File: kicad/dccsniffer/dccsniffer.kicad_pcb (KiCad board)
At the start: 2 copper layers, 53.3 x 48.3 mm, 14 parts, among them J1 , U1 6N137

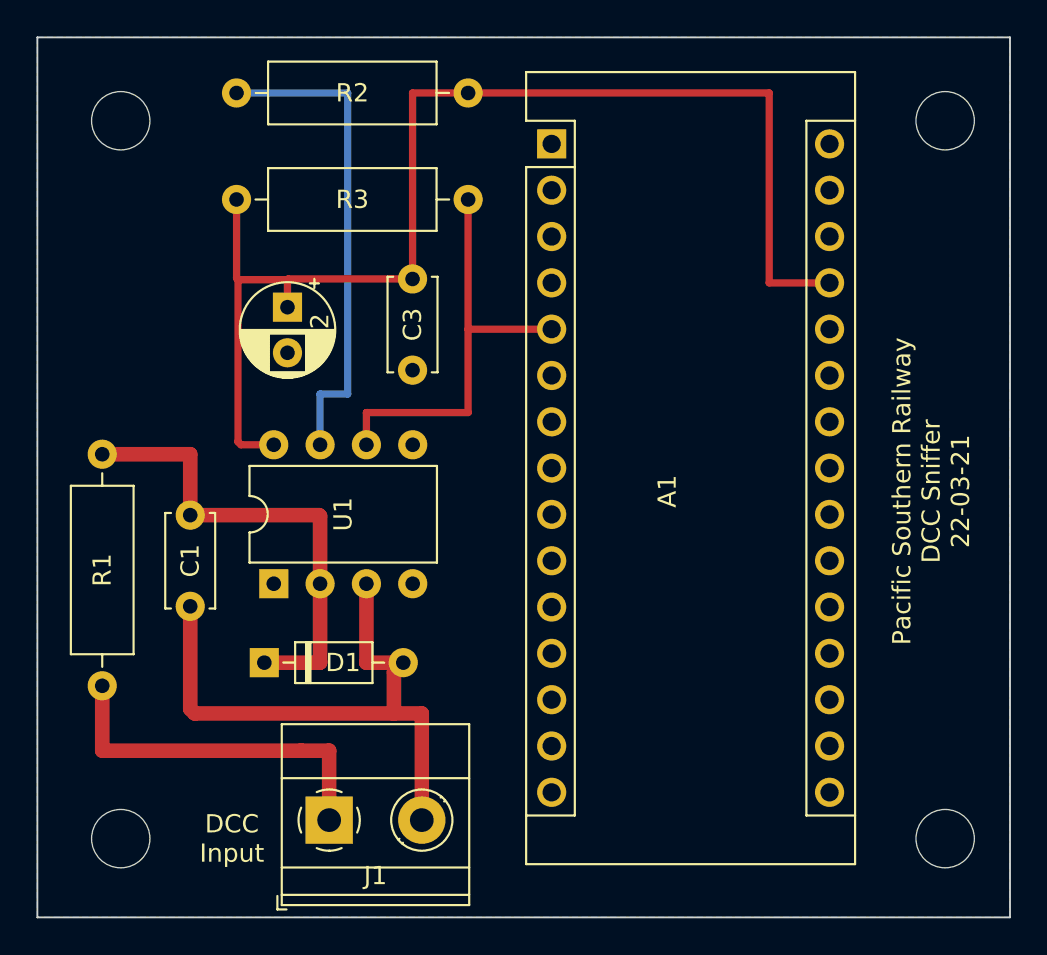
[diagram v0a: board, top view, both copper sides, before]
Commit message: updated dcc sniffer pcs, new arduino sketch for dcc server
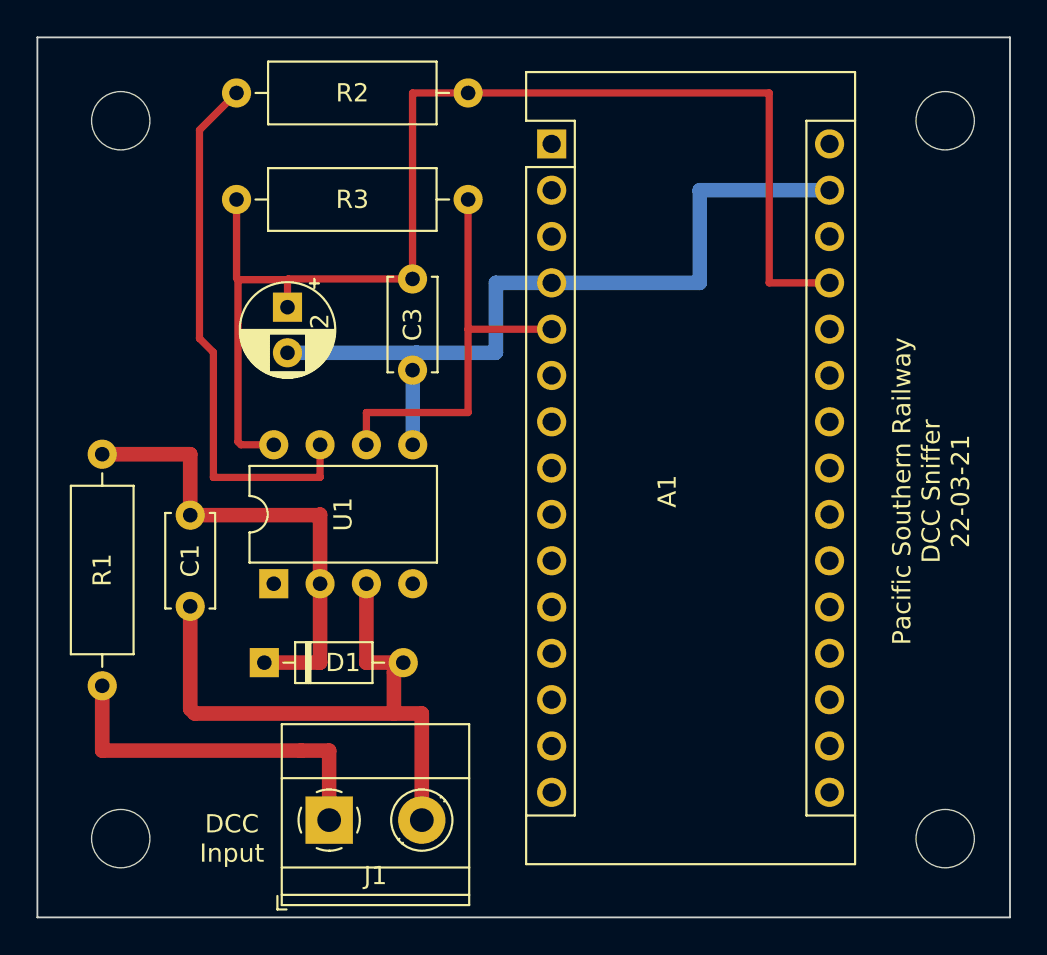
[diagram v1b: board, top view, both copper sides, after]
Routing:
- net GND: track 0.00 -> 43.8 mm
- net Net-(R2-Pad2): track 26.9 -> 29.9 mm
- removed copper zone on B.Cu, net GND
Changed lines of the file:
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@@
     (effects (font (size 1 1) (thickness 0.15)))
   )
+  (segment (start 117.104 35.042) (end 117.104 30.958) (width 0.8) (layer "B.Cu") (net 4))
+  (segment (start 110.236 29.996888) (end 117.323112 29.996888) (width 0.8) (layer "B.Cu") (net 4))
+  (segment (start 124.724 26.162) (end 132.842 26.162) (width 0.8) (layer "B.Cu") (net 4))
+  (segment (start 132.842 21.082) (end 139.964 21.082) (width 0.8) (layer "B.Cu") (net 4))
+  (segment (start 117.094 30.948) (end 117.094 30.226) (width 0.8) (layer "B.Cu") (net 4))
+  (segment (start 117.323112 29.996888) (end 121.641112 29.996888) (width 0.8) (layer "B.Cu") (net 4))
+  (segment (start 121.666 29.972) (end 121.666 26.162) (width 0.8) (layer "B.Cu") (net 4))
+  (segment (start 132.842 26.162) (end 132.842 21.082) (width 0.8) (layer "B.Cu") (net 4))
+  (segment (start 121.666 26.162) (end 124.724 26.162) (width 0.8) (layer "B.Cu") (net 4))
+  (segment (start 121.641112 29.996888) (end 121.666 29.972) (width 0.8) (layer "B.Cu") (net 4))
+  (segment (start 117.094 30.226) (end 117.323112 29.996888) (width 0.8) (layer "B.Cu") (net 4))
+  (segment (start 117.104 30.958) (end 117.094 30.948) (width 0.8) (layer "B.Cu") (net 4))
   (segment (start 124.724 28.702) (end 120.142 28.702) (width 0.4) (layer "F.Cu") (net 5))
   (segment (start 114.574 33.274) (end 120.142 33.274) (width 0.4) (layer "F.Cu") (net 5))
@@
   (segment (start 107.442 25.908) (end 107.522 25.988) (width 0.4) (layer "F.Cu") (net 27))
   (segment (start 110.236 25.988) (end 110.236 27.496888) (width 0.4) (layer "F.Cu") (net 27))
-  (segment (start 111.974 38.902) (end 112.024 38.952) (width 0.8) (layer "F.Cu") (net 30))
+  (segment (start 112.024 42.662) (end 112.024 38.872) (width 0.8) (layer "F.Cu") (net 30))
   (segment (start 112.014 46.99) (end 108.966 46.99) (width 0.8) (layer "F.Cu") (net 30))
   (segment (start 112.024 46.98) (end 112.014 46.99) (width 0.8) (layer "F.Cu") (net 30))
-  (segment (start 104.902 38.902) (end 111.974 38.902) (width 0.8) (layer "F.Cu") (net 30))
-  (segment (start 104.902 35.56) (end 104.902 38.902) (width 0.8) (layer "F.Cu") (net 30))
-  (segment (start 100.076 35.56) (end 104.902 35.56) (width 0.8) (layer "F.Cu") (net 30))
-  (segment (start 112.024 38.952) (end 112.024 42.662) (width 0.8) (layer "F.Cu") (net 30))
+  (segment (start 112.024 38.872) (end 111.994 38.902) (width 0.8) (layer "F.Cu") (net 30))
+  (segment (start 104.902 38.902) (end 104.902 35.56) (width 0.8) (layer "F.Cu") (net 30))
+  (segment (start 111.994 38.902) (end 104.902 38.902) (width 0.8) (layer "F.Cu") (net 30))
+  (segment (start 104.902 35.56) (end 100.076 35.56) (width 0.8) (layer "F.Cu") (net 30))
   (segment (start 104.862 38.862) (end 104.902 38.902) (width 0.8) (layer "F.Cu") (net 30))
   (segment (start 112.024 42.662) (end 112.024 46.98) (width 0.8) (layer "F.Cu") (net 30))
@@
   (segment (start 110.988 51.816) (end 100.076 51.816) (width 0.8) (layer "F.Cu") (net 32))
   (segment (start 112.522 51.816) (end 112.522 55.626) (width 0.8) (layer "F.Cu") (net 32))
-  (segment (start 112.024 32.268) (end 112.034 32.258) (width 0.4) (layer "B.Cu") (net 33))
-  (segment (start 112.024 35.042) (end 112.024 32.268) (width 0.4) (layer "B.Cu") (net 33))
-  (segment (start 113.538 32.258) (end 113.538 15.748) (width 0.4) (layer "B.Cu") (net 33))
-  (segment (start 113.538 15.748) (end 107.442 15.748) (width 0.4) (layer "B.Cu") (net 33))
-  (segment (start 112.034 32.258) (end 113.538 32.258) (width 0.4) (layer "B.Cu") (net 33))
-  (zone (net 4) (net_name "GND") (layer "B.Cu") (hatch edge 0.508)
-    (connect_pads (clearance 0.508))
-    (min_thickness 0.254) (filled_areas_thickness no)
-    (fill yes (thermal_gap 0.508) (thermal_bridge_width 0.508))
-    (polygon
-      (pts
-        (xy 149.86 60.96)
-        (xy 96.52 60.96)
-        (xy 96.52 12.7)
-        (xy 149.86 12.7)
-      )
-    )
-  )
+  (segment (start 106.172 29.972) (end 105.41 29.21) (width 0.4) (layer "F.Cu") (net 33))
+  (segment (start 112.014 36.83) (end 106.172 36.83) (width 0.4) (layer "F.Cu") (net 33))
+  (segment (start 106.172 36.83) (end 106.172 29.972) (width 0.4) (layer "F.Cu") (net 33))
+  (segment (start 112.024 36.82) (end 112.014 36.83) (width 0.4) (layer "F.Cu") (net 33))
+  (segment (start 105.41 17.78) (end 107.442 15.748) (width 0.4) (layer "F.Cu") (net 33))
+  (segment (start 112.024 35.042) (end 112.024 36.82) (width 0.4) (layer "F.Cu") (net 33))
+  (segment (start 105.41 29.21) (end 105.41 17.78) (width 0.4) (layer "F.Cu") (net 33))
 )
